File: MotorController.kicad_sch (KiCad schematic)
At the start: 0 parts

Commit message: heheheheh
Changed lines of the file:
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@@
 	(generator_version "9.0")
 	(paper "A4")
+	(hierarchical_label "DC-"
+		(shape input)
+		(at 102.87 96.52 0)
+		(effects
+			(font
+				(size 1.27 1.27)
+			)
+			(justify left)
+		)
+	)
 	(hierarchical_label "+ICAN"
 		(shape input)
@@
 		)
 	)
+	(hierarchical_label "DC+"
+		(shape input)
+		(at 102.87 92.71 0)
+		(effects
+			(font
+				(size 1.27 1.27)
+			)
+			(justify left)
+		)
+	)
+	(hierarchical_label "PhaseB"
+		(shape output)
+		(at 102.87 104.775 0)
+		(effects
+			(font
+				(size 1.27 1.27)
+			)
+			(justify left)
+		)
+	)
 	(hierarchical_label "-ICAN"
 		(shape input)
@@
 		(effects
 			(font
+				(size 1.27 1.27)
+			)
+			(justify left)
+		)
+	)
+	(hierarchical_label "PhaseA"
+		(shape output)
+		(at 102.87 100.33 0)
+		(effects
+			(font
+				(size 1.27 1.27)
+			)
+			(justify left)
+		)
+	)
+	(hierarchical_label "PhaseC"
+		(shape output)
+		(at 102.87 108.585 0)
+		(effects
+			(font

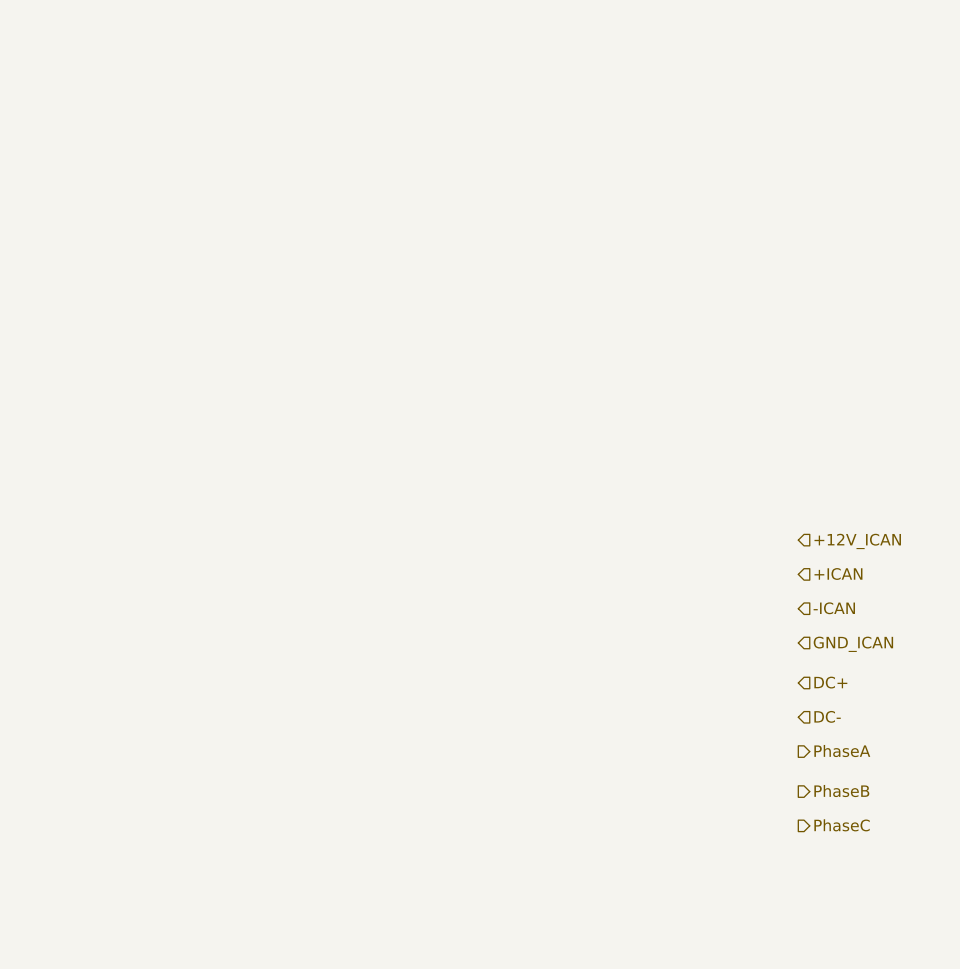
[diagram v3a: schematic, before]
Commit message: initial HV diagram changes
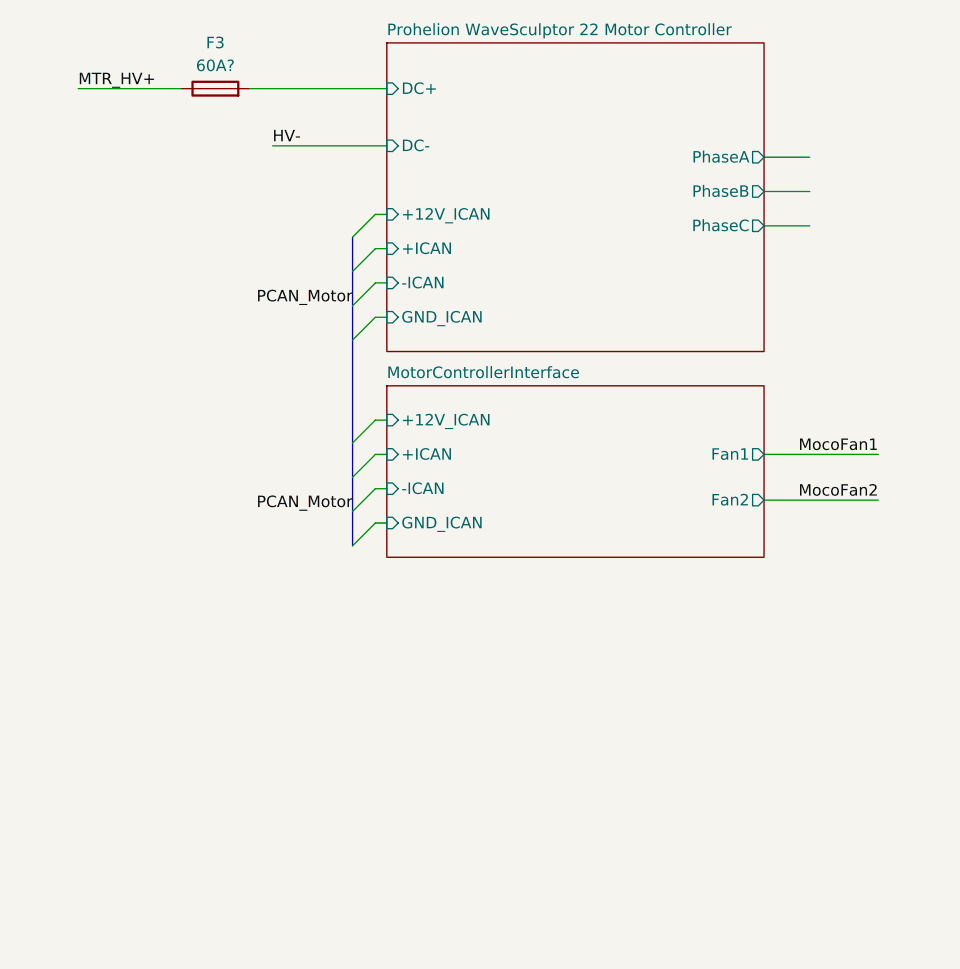
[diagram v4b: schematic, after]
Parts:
- added F3: 60A?, symbol Device:Fuse
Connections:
- new net MTR_HV+: F3.1
- new net Prohelion WaveSculptor 22 Motor Controller/DC+: F3.2
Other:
- added sheet MotorControllerInterface (MotorControllerInterface.kicad_sch)
- added sheet Prohelion WaveSculptor 22 Motor Controller (WaveSculptor.kicad_sch)

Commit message: reorganized top
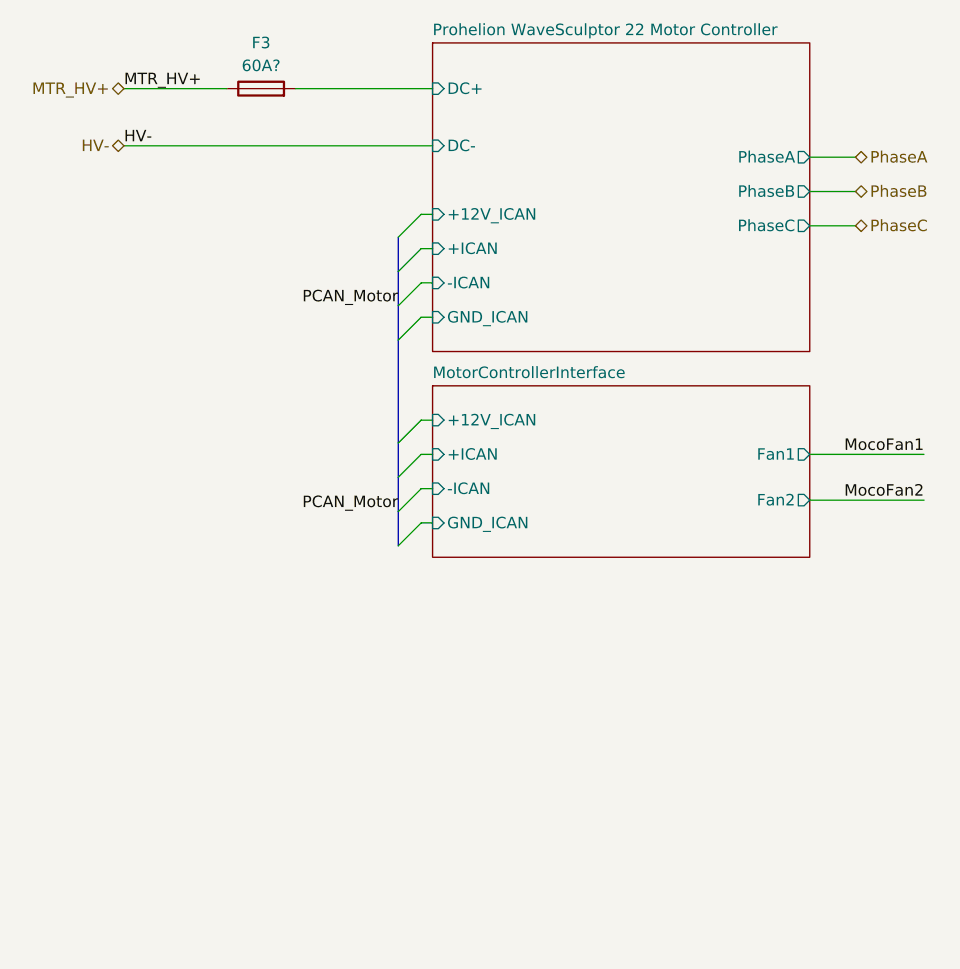
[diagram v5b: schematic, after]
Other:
- moved on the sheet: F3

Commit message: Updated Controls + Telemetry
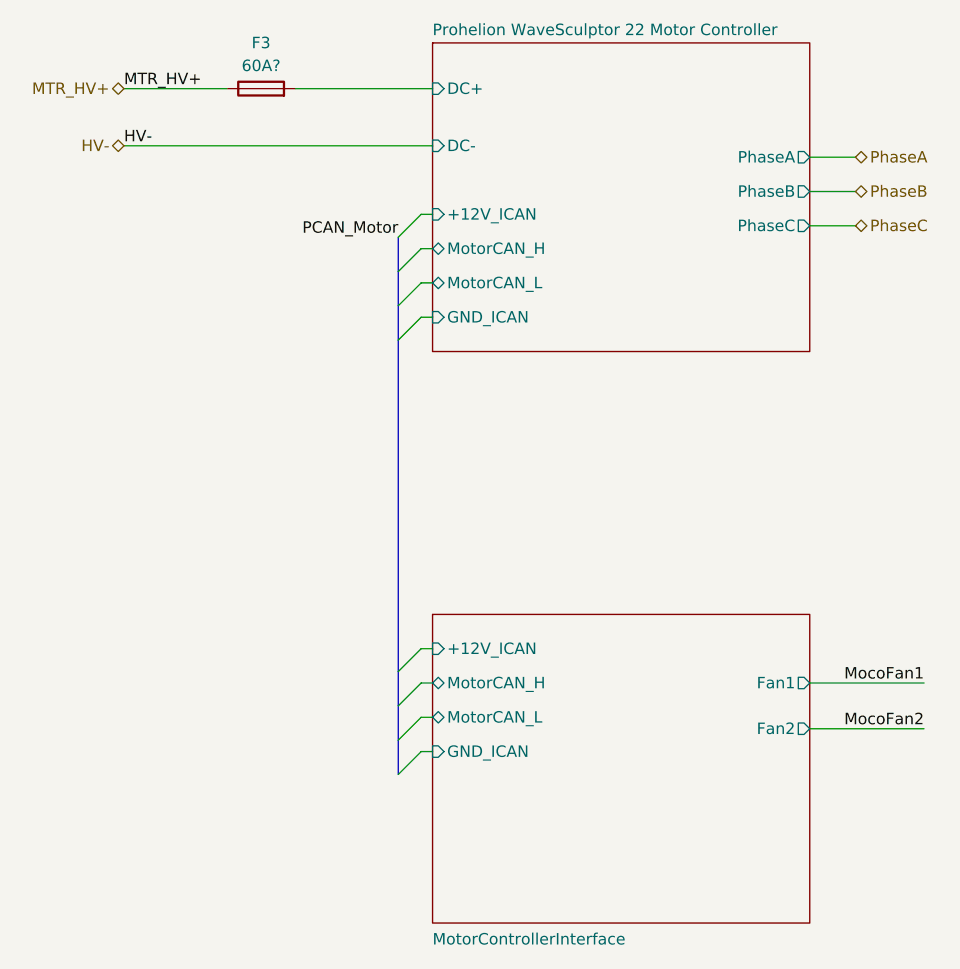
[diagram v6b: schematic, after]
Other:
- sheet MotorControllerInterface ports: added MotorCAN_H, MotorCAN_L; removed +ICAN, -ICAN
- sheet Prohelion WaveSculptor 22 Motor Controller ports: added MotorCAN_H, MotorCAN_L; removed +ICAN, -ICAN
